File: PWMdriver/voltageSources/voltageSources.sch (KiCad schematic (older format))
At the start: 7 parts

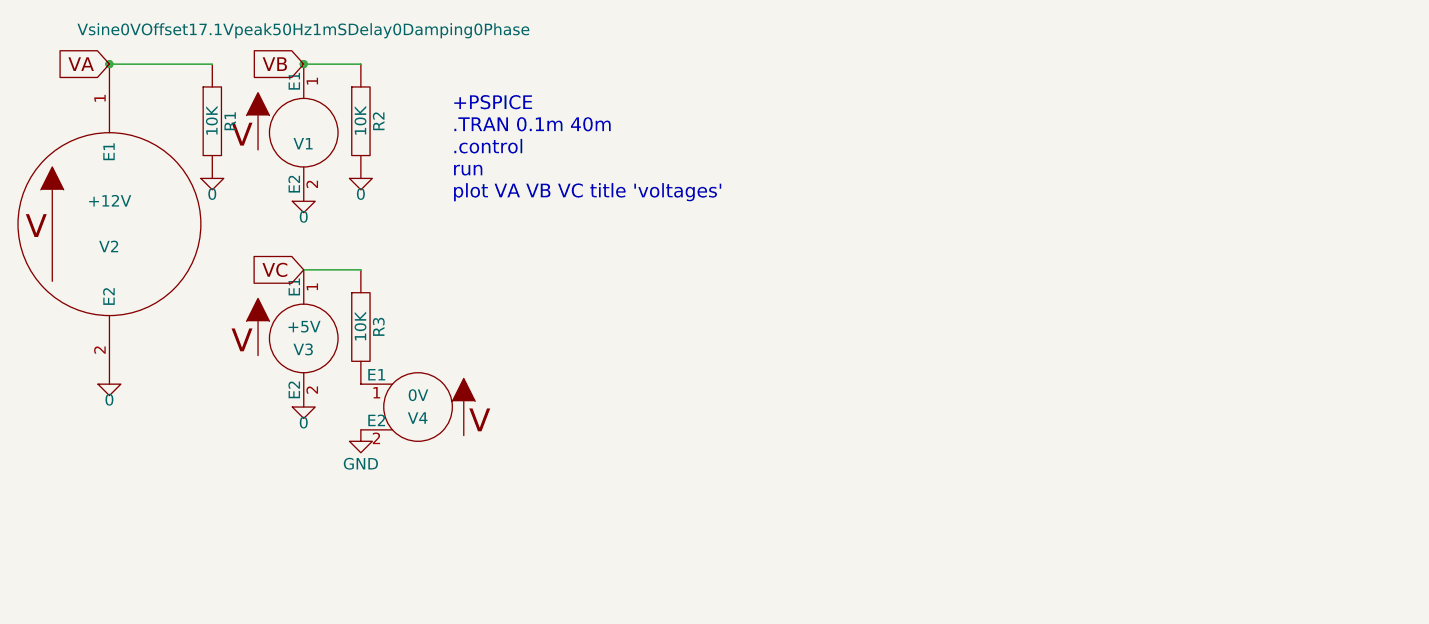
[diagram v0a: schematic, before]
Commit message: added Vpulse source
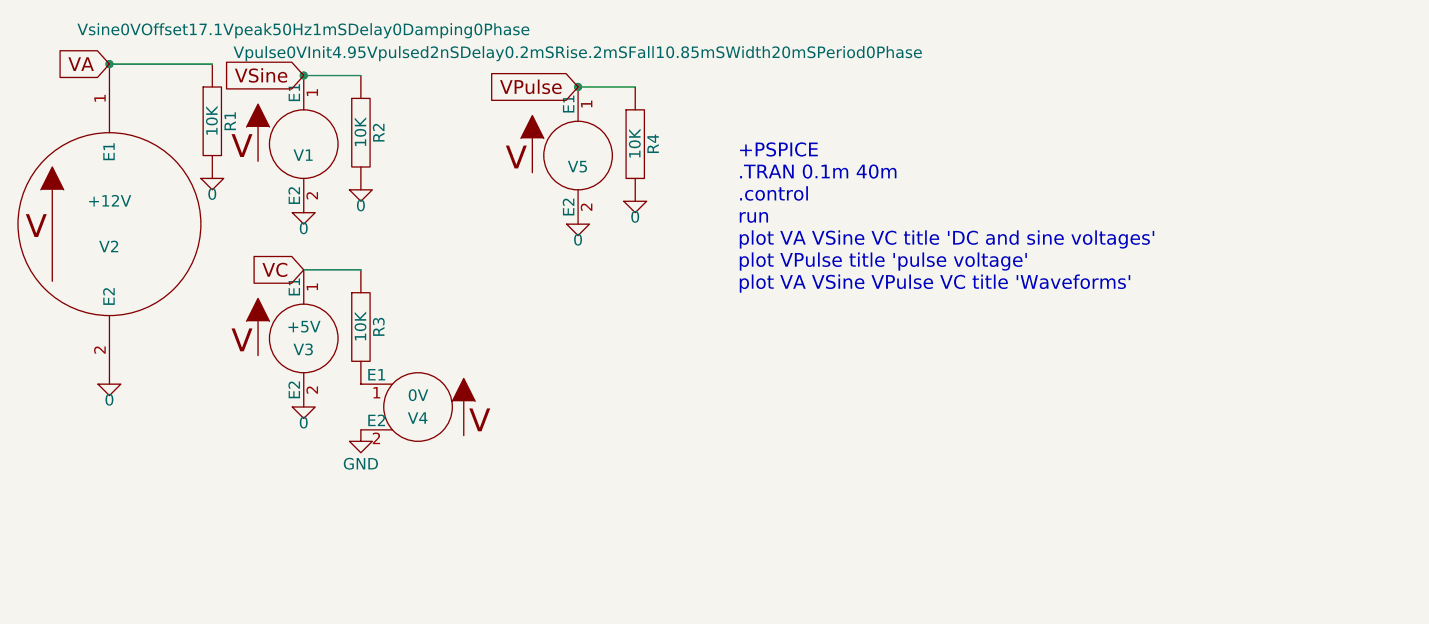
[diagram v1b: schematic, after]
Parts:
- removed V1: Vsine0VOffset17.1Vpeak50Hz1mSDelay0Damping0Phase, symbol Vsine
- added R4: 10K, symbol R
- added V1: Vsine0VOffset17.1Vpeak50Hz1mSDelay0Damping0Phase, symbol Vsine0VOffset17.1Vpeak50Hz1mSDelay0Damping0Phase
- added V5: Vpulse0VInit4.95Vpulsed2nSDelay0.2mSRise.2mSFall1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, symbol Vpulse0VInit4.95Vpulsed2nSDelay0.2mSRise.2mSFall10.85mSWidth20mSPeriod0Phase
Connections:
- net 0: now also R4.2, V1.2 (E2), V5.2 (E2)
- net VB renamed VSine
- net VSine: now also V1.1 (E1)
- new net VPulse: R4.1, V5.1 (E1)
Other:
- note added: "+PSPICE\n.TRAN 0.1m 40m\n.control\nrun\nplot VA VSine VC title 'DC and sine voltages'\nplot VPulse title 'pulse voltage'\nplot VA VSine VPulse VC title 'Waveforms'\n"
- note removed: "+PSPICE\n.TRAN 0.1m 40m\n.control\nrun\nplot VA VB VC title 'voltages'"
- moved on the sheet: R2

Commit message: update to voltageSources
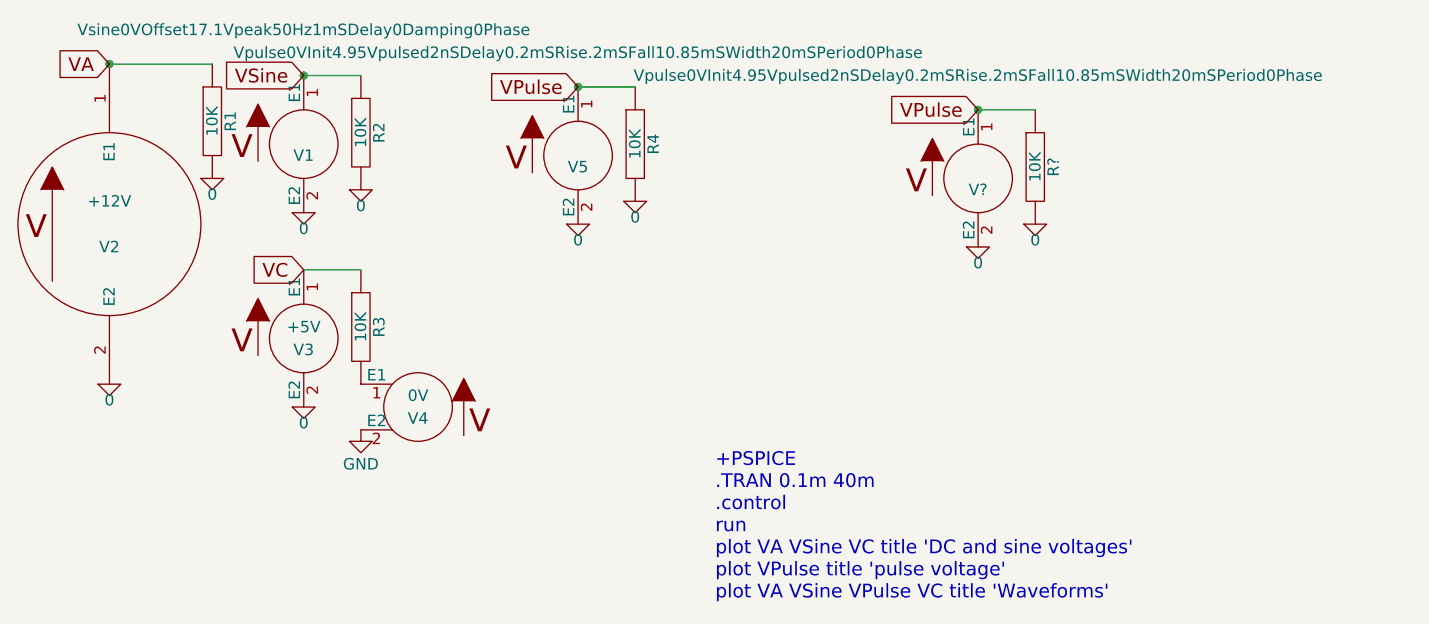
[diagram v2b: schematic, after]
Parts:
- added R?: 10K, symbol R
- added V?: Vpulse0VInit4.95Vpulsed2nSDelay0.2mSRise.2mSFall1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, symbol Vpulse0VInit4.95Vpulsed2nSDelay0.2mSRise.2mSFall10.85mSWidth20mSPeriod0Phase
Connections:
- net 0: now also R?.2, V?.2 (E2)
- net VPulse: now also R?.1, V?.1 (E1)
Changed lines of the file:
@@
 	1    0    0    -1
 $EndComp
-Text Notes 4400 2050 0    60   ~ 0
+Text Notes 4300 3400 0    60   ~ 0
 +PSPICE\n.TRAN 0.1m 40m\n.control\nrun\nplot VA VSine VC title 'DC and sine voltages'\nplot VPulse title 'pulse voltage'\nplot VA VSine VPulse VC title 'Waveforms'\n
 Connection ~ 1650 1050
@@
 EndData
 $EndBitmap
+Text GLabel 5450 1250 0    60   Input ~ 0
+VPulse
+$Comp
+L 0 #GND?
+U 1 1 5B110CCA
+P 5450 1850
+F 0 "#GND?" H 5450 1750 50  0001 C CNN
+F 1 "0" H 5450 1780 50  0000 C CNN
+F 2 "" H 5450 1850 50  0001 C CNN
+F 3 "" H 5450 1850 50  0001 C CNN
+	1    5450 1850
+	1    0    0    -1
+$EndComp
+Connection ~ 5450 1250
+$Comp
+L R R?
+U 1 1 5B110CD1
+P 5700 1500
+F 0 "R?" V 5780 1500 50  0000 C CNN
+F 1 "10K" V 5700 1500 50  0000 C CNN
+F 2 "" H 5700 1500 50  0001 C CNN
+F 3 "" H 5700 1500 50  0001 C CNN
+	1    5700 1500
+	1    0    0    -1
+$EndComp
+Wire Wire Line
+	5700 1250 5450 1250
+$Comp
+L 0 #GND?
+U 1 1 5B110CD8
+P 5700 1750
+F 0 "#GND?" H 5700 1650 50  0001 C CNN
+F 1 "0" H 5700 1680 50  0000 C CNN
+F 2 "" H 5700 1750 50  0001 C CNN
+F 3 "" H 5700 1750 50  0001 C CNN
+	1    5700 1750
+	1    0    0    -1
+$EndComp
+$Comp
+L Vpulse0VInit4.95Vpulsed2nSDelay0.2mSRise.2mSFall10.85mSWidth20mSPeriod0Phase V?
+U 1 1 5B110CDE
+P 5450 1550
+F 0 "V?" H 5450 1500 50  0000 C CNN
+F 1 "Vpulse0VInit4.95Vpulsed2nSDelay0.2mSRise.2mSFall10.85mSWidth20mSPeriod0Phase" H 5450 2000 50  0000 C CNN
+F 2 "" H 5450 1550 50  0001 C CNN
+F 3 "" H 5450 1550 50  0001 C CNN
+	1    5450 1550
+	1    0    0    -1
+$EndComp
 $EndSCHEMATC

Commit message: added VCVS Voltage Controlled Voltage Source
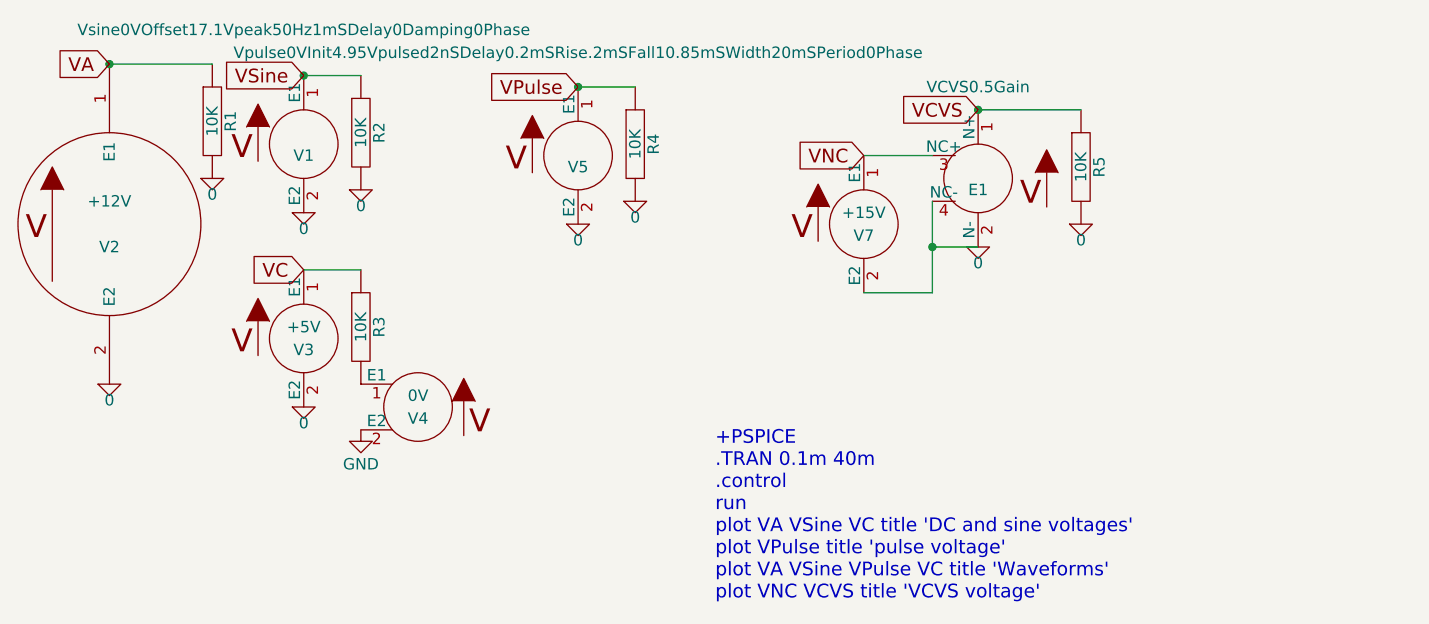
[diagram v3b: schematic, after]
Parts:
- removed V?: Vpulse0VInit4.95Vpulsed2nSDelay0.2mSRise.2mSFall1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, symbol Vpulse0VInit4.95Vpulsed2nSDelay0.2mSRise.2mSFall10.85mSWidth20mSPeriod0Phase
- added E1: VCVS0.5Gain, symbol VCVS0.5Gain
- added V7: +15V, symbol +5V
- gave numbers to parts that had none: 1
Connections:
- net 0: now also E1.2 (N-), E1.4 (NC-), V7.2 (E2)
- net VPulse: no longer R5.1
- new net VCVS: E1.1 (N+), R5.1
- new net VNC: E1.3 (NC+), V7.1 (E1)
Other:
- note added: "+PSPICE\n.TRAN 0.1m 40m\n.control\nrun\nplot VA VSine VC title 'DC and sine voltages'\nplot VPulse title 'pulse voltage'\nplot VA VSine VPulse VC title 'Waveforms'\nplot VNC VCVS title 'VCVS voltage'\n"
- note removed: "+PSPICE\n.TRAN 0.1m 40m\n.control\nrun\nplot VA VSine VC title 'DC and sine voltages'\nplot VPulse title 'pulse voltage'\nplot VA VSine VPulse VC title 'Waveforms'\n"
- moved on the sheet: R5
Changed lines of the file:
@@
 VSine
 $Comp
-L 0 #GND01
+L 0 #GND4
 U 1 1 5B0E04BE
 P 2500 1700
-F 0 "#GND01" H 2500 1600 50  0001 C CNN
+F 0 "#GND4" H 2500 1600 50  0001 C CNN
 F 1 "0" H 2500 1630 50  0000 C CNN
 F 2 "" H 2500 1700 50  0001 C CNN
@@
 $EndComp
 $Comp
-L 0 #GND02
+L 0 #GND8
 U 1 1 5B0E04D6
 P 1650 2450
-F 0 "#GND02" H 1650 2350 50  0001 C CNN
+F 0 "#GND8" H 1650 2350 50  0001 C CNN
 F 1 "0" H 1650 2380 50  0000 C CNN
 F 2 "" H 1650 2450 50  0001 C CNN
@@
 $EndComp
 Text Notes 4300 3400 0    60   ~ 0
-+PSPICE\n.TRAN 0.1m 40m\n.control\nrun\nplot VA VSine VC title 'DC and sine voltages'\nplot VPulse title 'pulse voltage'\nplot VA VSine VPulse VC title 'Waveforms'\n
++PSPICE\n.TRAN 0.1m 40m\n.control\nrun\nplot VA VSine VC title 'DC and sine voltages'\nplot VPulse title 'pulse voltage'\nplot VA VSine VPulse VC title 'Waveforms'\nplot VNC VCVS title 'VCVS voltage'\n
 Connection ~ 1650 1050
 Connection ~ 2500 1100
@@
 	2100 1050 1650 1050
 $Comp
-L 0 #GND03
+L 0 #GND1
 U 1 1 5B0E06D9
 P 2100 1550
-F 0 "#GND03" H 2100 1450 50  0001 C CNN
+F 0 "#GND1" H 2100 1450 50  0001 C CNN
 F 1 "0" H 2100 1480 50  0000 C CNN
 F 2 "" H 2100 1550 50  0001 C CNN
@@
 $EndComp
 $Comp
-L 0 #GND04
+L 0 #GND2
 U 1 1 5B0E06F0
 P 2750 1600
-F 0 "#GND04" H 2750 1500 50  0001 C CNN
+F 0 "#GND2" H 2750 1500 50  0001 C CNN
 F 1 "0" H 2750 1530 50  0000 C CNN
 F 2 "" H 2750 1600 50  0001 C CNN
@@
 	2500 1950 2750 1950
 $Comp
-L 0 #GND05
+L 0 #GND9
 U 1 1 5B0E0BAA
 P 2500 2550
-F 0 "#GND05" H 2500 2450 50  0001 C CNN
+F 0 "#GND9" H 2500 2450 50  0001 C CNN
 F 1 "0" H 2500 2480 50  0000 C CNN
 F 2 "" H 2500 2550 50  0001 C CNN
@@
 $EndComp
 $Comp
-L GND #PWR06
+L GND #PWR1
 U 1 1 5B0EA963
 P 2750 2650
-F 0 "#PWR06" H 2750 2400 50  0001 C CNN
+F 0 "#PWR1" H 2750 2400 50  0001 C CNN
 F 1 "GND" H 2750 2500 50  0000 C CNN
 F 2 "" H 2750 2650 50  0001 C CNN
@@
 VPulse
 $Comp
-L 0 #GND07
+L 0 #GND5
 U 1 1 5B10EAA6
 P 3700 1750
-F 0 "#GND07" H 3700 1650 50  0001 C CNN
+F 0 "#GND5" H 3700 1650 50  0001 C CNN
 F 1 "0" H 3700 1680 50  0000 C CNN
 F 2 "" H 3700 1750 50  0001 C CNN
@@
 	3950 1150 3700 1150
 $Comp
-L 0 #GND08
+L 0 #GND3
 U 1 1 5B10EAB4
 P 3950 1650
-F 0 "#GND08" H 3950 1550 50  0001 C CNN
+F 0 "#GND3" H 3950 1550 50  0001 C CNN
 F 1 "0" H 3950 1580 50  0000 C CNN
 F 2 "" H 3950 1650 50  0001 C CNN
@@
 $EndBitmap
 Text GLabel 5450 1250 0    60   Input ~ 0
-VPulse
-$Comp
-L 0 #GND?
+VCVS
+$Comp
+L 0 #GND7
 U 1 1 5B110CCA
 P 5450 1850
-F 0 "#GND?" H 5450 1750 50  0001 C CNN
+F 0 "#GND7" H 5450 1750 50  0001 C CNN
 F 1 "0" H 5450 1780 50  0000 C CNN
 F 2 "" H 5450 1850 50  0001 C CNN
@@
 Connection ~ 5450 1250
 $Comp
-L R R?
+L R R5
 U 1 1 5B110CD1
-P 5700 1500
-F 0 "R?" V 5780 1500 50  0000 C CNN
-F 1 "10K" V 5700 1500 50  0000 C CNN
-F 2 "" H 5700 1500 50  0001 C CNN
-F 3 "" H 5700 1500 50  0001 C CNN
-	1    5700 1500
-	1    0    0    -1
-$EndComp
-Wire Wire Line
-	5700 1250 5450 1250
-$Comp
-L 0 #GND?
+P 5900 1500
+F 0 "R5" V 5980 1500 50  0000 C CNN
+F 1 "10K" V 5900 1500 50  0000 C CNN
+F 2 "" H 5900 1500 50  0001 C CNN
+F 3 "" H 5900 1500 50  0001 C CNN
+	1    5900 1500
+	1    0    0    -1
+$EndComp
+Wire Wire Line
+	5900 1250 5450 1250
+$Comp
+L 0 #GND6
 U 1 1 5B110CD8
-P 5700 1750
-F 0 "#GND?" H 5700 1650 50  0001 C CNN
-F 1 "0" H 5700 1680 50  0000 C CNN
-F 2 "" H 5700 1750 50  0001 C CNN
-F 3 "" H 5700 1750 50  0001 C CNN
-	1    5700 1750
-	1    0    0    -1
-$EndComp
-$Comp
-L Vpulse0VInit4.95Vpulsed2nSDelay0.2mSRise.2mSFall10.85mSWidth20mSPeriod0Phase V?
-U 1 1 5B110CDE
+P 5900 1750
+F 0 "#GND6" H 5900 1650 50  0001 C CNN
+F 1 "0" H 5900 1680 50  0000 C CNN
+F 2 "" H 5900 1750 50  0001 C CNN
+F 3 "" H 5900 1750 50  0001 C CNN
+	1    5900 1750
+	1    0    0    -1
+$EndComp
+Wire Wire Line
+	5250 1650 5250 2050
+Wire Wire Line
+	5250 1850 5450 1850
+$Comp
+L +5V V7
+U 1 1 5B1295A2
+P 4950 1750
+F 0 "V7" H 4950 1700 50  0000 C CNN
+F 1 "+15V" H 4950 1800 50  0000 C CNN
+F 2 "" H 4950 1750 50  0001 C CNN
+F 3 "" H 4950 1750 50  0001 C CNN
+	1    4950 1750
+	1    0    0    -1
+$EndComp
+Wire Wire Line
+	5250 1450 4950 1450
+Wire Wire Line
+	5250 2050 4950 2050
+Connection ~ 5250 1850
+Text GLabel 4950 1450 0    60   Input ~ 0
+VNC
+$Comp
+L VCVS0.5Gain E1
+U 1 1 5B12A85C
 P 5450 1550
-F 0 "V?" H 5450 1500 50  0000 C CNN
-F 1 "Vpulse0VInit4.95Vpulsed2nSDelay0.2mSRise.2mSFall10.85mSWidth20mSPeriod0Phase" H 5450 2000 50  0000 C CNN
+F 0 "E1" H 5450 1500 50  0000 C CNN
+F 1 "VCVS0.5Gain" H 5450 1950 50  0000 C CNN
 F 2 "" H 5450 1550 50  0001 C CNN
 F 3 "" H 5450 1550 50  0001 C CNN
